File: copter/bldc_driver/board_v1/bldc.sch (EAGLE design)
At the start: 86 parts, among them IC1 LM339APWR, IC2 7411, IC3 7411, IC4 CD4051BPWR, IC5 FAN7388, Y1 16MHz

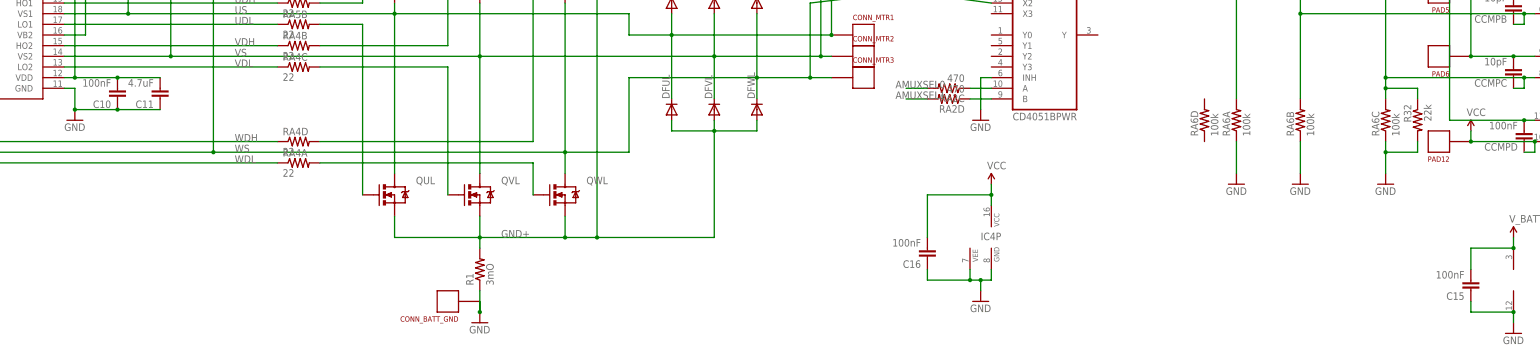
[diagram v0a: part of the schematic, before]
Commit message: simple arduino makefile
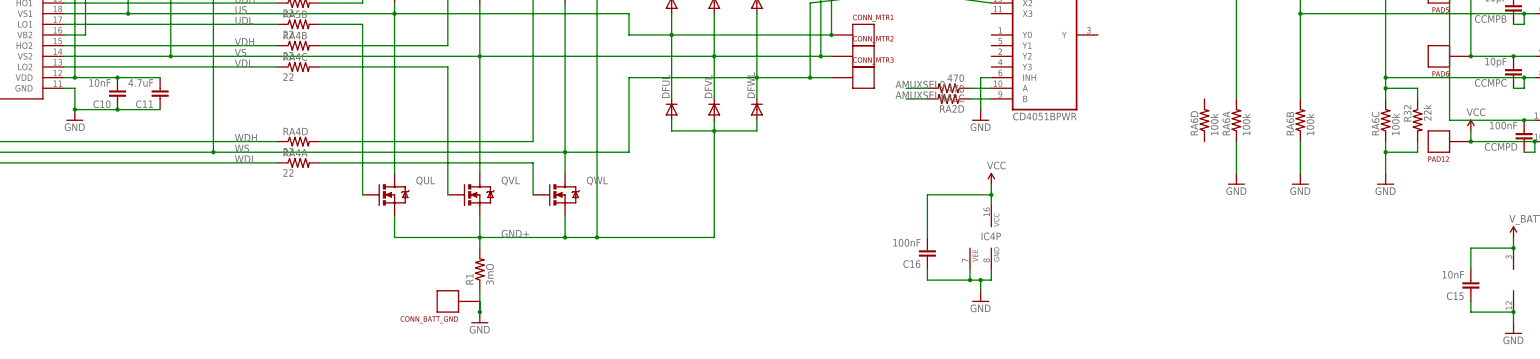
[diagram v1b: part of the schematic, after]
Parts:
- C10, C15: value 100nF -> 10nF
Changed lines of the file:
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@@
 <grid distance="0.1" unitdist="inch" unit="inch" style="lines" multiple="1" display="no" altdistance="0.01" altunitdist="inch" altunit="inch"/>
 <layers>
-<layer number="1" name="Top" color="4" fill="1" visible="yes" active="no"/>
-<layer number="16" name="Bottom" color="1" fill="1" visible="yes" active="no"/>
-<layer number="17" name="Pads" color="2" fill="1" visible="yes" active="no"/>
-<layer number="18" name="Vias" color="2" fill="1" visible="yes" active="no"/>
-<layer number="19" name="Unrouted" color="6" fill="1" visible="yes" active="no"/>
-<layer number="20" name="Dimension" color="15" fill="1" visible="yes" active="no"/>
-<layer number="21" name="tPlace" color="16" fill="1" visible="yes" active="no"/>
-<layer number="22" name="bPlace" color="14" fill="1" visible="yes" active="no"/>
-<layer number="23" name="tOrigins" color="15" fill="1" visible="yes" active="no"/>
-<layer number="24" name="bOrigins" color="15" fill="1" visible="yes" active="no"/>
-<layer number="25" name="tNames" color="7" fill="1" visible="yes" active="no"/>
-<layer number="26" name="bNames" color="7" fill="1" visible="yes" active="no"/>
-<layer number="27" name="tValues" color="7" fill="1" visible="yes" active="no"/>
-<layer number="28" name="bValues" color="7" fill="1" visible="yes" active="no"/>
+<layer number="1" name="Top" color="4" fill="1" visible="no" active="no"/>
+<layer number="16" name="Bottom" color="1" fill="1" visible="no" active="no"/>
+<layer number="17" name="Pads" color="2" fill="1" visible="no" active="no"/>
+<layer number="18" name="Vias" color="2" fill="1" visible="no" active="no"/>
+<layer number="19" name="Unrouted" color="6" fill="1" visible="no" active="no"/>
+<layer number="20" name="Dimension" color="15" fill="1" visible="no" active="no"/>
+<layer number="21" name="tPlace" color="16" fill="1" visible="no" active="no"/>
+<layer number="22" name="bPlace" color="14" fill="1" visible="no" active="no"/>
+<layer number="23" name="tOrigins" color="15" fill="1" visible="no" active="no"/>
+<layer number="24" name="bOrigins" color="15" fill="1" visible="no" active="no"/>
+<layer number="25" name="tNames" color="7" fill="1" visible="no" active="no"/>
+<layer number="26" name="bNames" color="7" fill="1" visible="no" active="no"/>
+<layer number="27" name="tValues" color="7" fill="1" visible="no" active="no"/>
+<layer number="28" name="bValues" color="7" fill="1" visible="no" active="no"/>
 <layer number="29" name="tStop" color="7" fill="3" visible="no" active="no"/>
 <layer number="30" name="bStop" color="7" fill="6" visible="no" active="no"/>
@@
 <layer number="35" name="tGlue" color="7" fill="4" visible="no" active="no"/>
 <layer number="36" name="bGlue" color="7" fill="5" visible="no" active="no"/>
-<layer number="37" name="tTest" color="7" fill="1" visible="yes" active="no"/>
-<layer number="38" name="bTest" color="7" fill="1" visible="yes" active="no"/>
+<layer number="37" name="tTest" color="7" fill="1" visible="no" active="no"/>
+<layer number="38" name="bTest" color="7" fill="1" visible="no" active="no"/>
 <layer number="39" name="tKeepout" color="4" fill="11" visible="no" active="no"/>
 <layer number="40" name="bKeepout" color="1" fill="11" visible="no" active="no"/>
@@
 <layer number="44" name="Drills" color="7" fill="1" visible="no" active="no"/>
 <layer number="45" name="Holes" color="7" fill="1" visible="no" active="no"/>
-<layer number="46" name="Milling" color="3" fill="1" visible="yes" active="no"/>
-<layer number="47" name="Measures" color="7" fill="1" visible="yes" active="no"/>
-<layer number="48" name="Document" color="7" fill="1" visible="yes" active="no"/>
-<layer number="49" name="Reference" color="7" fill="1" visible="yes" active="no"/>
-<layer number="50" name="dxf" color="7" fill="1" visible="yes" active="no"/>
-<layer number="51" name="tDocu" color="6" fill="1" visible="yes" active="no"/>
-<layer number="52" name="bDocu" color="7" fill="1" visible="yes" active="no"/>
-<layer number="53" name="tGND_GNDA" color="7" fill="9" visible="yes" active="no"/>
-<layer number="54" name="bGND_GNDA" color="1" fill="9" visible="yes" active="no"/>
-<layer number="56" name="wert" color="7" fill="1" visible="yes" active="no"/>
+<layer number="46" name="Milling" color="3" fill="1" visible="no" active="no"/>
+<layer number="47" name="Measures" color="7" fill="1" visible="no" active="no"/>
+<layer number="48" name="Document" color="7" fill="1" visible="no" active="no"/>
+<layer number="49" name="Reference" color="7" fill="1" visible="no" active="no"/>
+<layer number="50" name="dxf" color="7" fill="1" visible="no" active="no"/>
+<layer number="51" name="tDocu" color="6" fill="1" visible="no" active="no"/>
+<layer number="52" name="bDocu" color="7" fill="1" visible="no" active="no"/>
+<layer number="53" name="tGND_GNDA" color="7" fill="9" visible="no" active="no"/>
+<layer number="54" name="bGND_GNDA" color="1" fill="9" visible="no" active="no"/>
+<layer number="56" name="wert" color="7" fill="1" visible="no" active="no"/>
 <layer number="91" name="Nets" color="2" fill="1" visible="yes" active="yes"/>
 <layer number="92" name="Busses" color="1" fill="1" visible="yes" active="yes"/>
@@
 <part name="GND11" library="SparkFun-Aesthetics" deviceset="GND" device=""/>
 <part name="GND12" library="SparkFun-Aesthetics" deviceset="GND" device=""/>
-<part name="C10" library="SparkFun-Capacitors" deviceset="10NF-CER" device="" value="100nF"/>
+<part name="C10" library="SparkFun-Capacitors" deviceset="10NF-CER" device="" value="10nF"/>
 <part name="C11" library="SparkFun-Capacitors" deviceset="22UF-6.3V-20%(0805)" device="" value="4.7uF"/>
 <part name="C12" library="SparkFun-Capacitors" deviceset="22UF-6.3V-20%(0805)" device="" value="4.7uF">
@@
 <part name="GND21" library="SparkFun-Aesthetics" deviceset="GND" device=""/>
 <part name="SUPPLY12" library="SparkFun-Aesthetics" deviceset="V_BATT" device=""/>
-<part name="C15" library="SparkFun-Capacitors" deviceset="10NF-CER" device="" value="100nF"/>
+<part name="C15" library="SparkFun-Capacitors" deviceset="10NF-CER" device="" value="10nF"/>
 <part name="SUPPLY13" library="SparkFun-Aesthetics" deviceset="VCC" device=""/>
 <part name="R24" library="SparkFun-Resistors" deviceset="RESISTOR" device="0603-RES" value="10k"/>

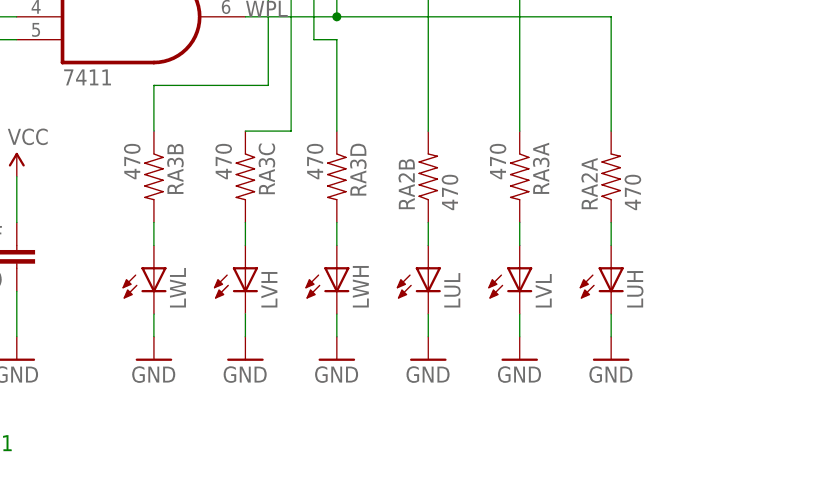
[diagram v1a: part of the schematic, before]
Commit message: fix some of the names in the bldc eagle files; update driver firmware to work with new board
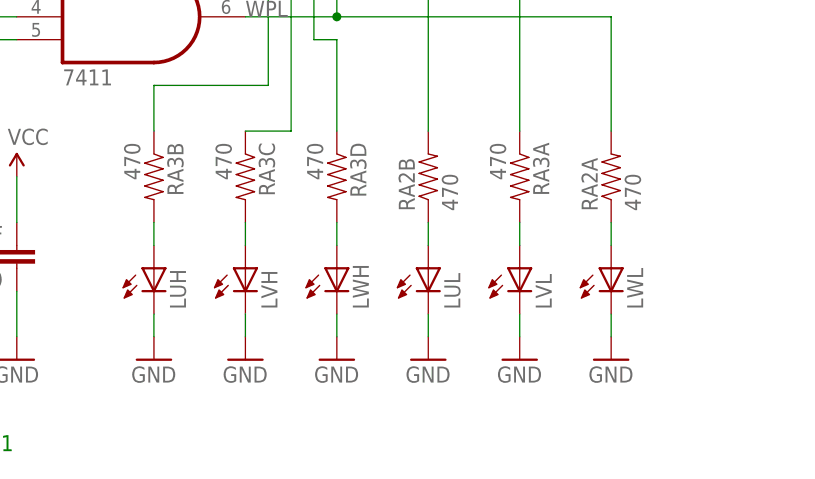
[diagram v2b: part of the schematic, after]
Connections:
- net N$8: now also LUH.A; no longer LWL.A
- net N$9: now also LWL.A; no longer LUH.A
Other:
- moved on the sheet: LUH, LWL
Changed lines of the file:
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@@
 <part name="SUPPLY10" library="SparkFun-Aesthetics" deviceset="V_BATT" device=""/>
 <part name="SUPPLY11" library="SparkFun-Aesthetics" deviceset="V_BATT" device=""/>
-<part name="LUH" library="kmod" deviceset="LED" device="0603" value=""/>
+<part name="LWL" library="kmod" deviceset="LED" device="0603" value=""/>
 <part name="GND15" library="SparkFun-Aesthetics" deviceset="GND" device=""/>
 <part name="LVH" library="kmod" deviceset="LED" device="0603" value=""/>
@@
 <part name="LVL" library="kmod" deviceset="LED" device="0603" value=""/>
 <part name="GND19" library="SparkFun-Aesthetics" deviceset="GND" device=""/>
-<part name="LWL" library="kmod" deviceset="LED" device="0603" value=""/>
+<part name="LUH" library="kmod" deviceset="LED" device="0603" value=""/>
 <part name="GND20" library="SparkFun-Aesthetics" deviceset="GND" device=""/>
 <part name="IC1" library="kmod" deviceset="LM339" device="" value="LM339APWR"/>
@@
 <instance part="SUPPLY10" gate="G$1" x="345.44" y="83.82"/>
 <instance part="SUPPLY11" gate="G$1" x="401.32" y="68.58"/>
-<instance part="LUH" gate="G$1" x="223.52" y="-17.78"/>
+<instance part="LWL" gate="G$1" x="223.52" y="-17.78"/>
 <instance part="GND15" gate="1" x="172.72" y="-27.94"/>
 <instance part="LVH" gate="G$1" x="182.88" y="-17.78"/>
@@
 <instance part="LVL" gate="G$1" x="213.36" y="-17.78"/>
 <instance part="GND19" gate="1" x="213.36" y="-27.94"/>
-<instance part="LWL" gate="G$1" x="172.72" y="-17.78"/>
+<instance part="LUH" gate="G$1" x="172.72" y="-17.78"/>
 <instance part="GND20" gate="1" x="223.52" y="-27.94"/>
 <instance part="IC1" gate="A" x="604.52" y="76.2"/>
@@
 </segment>
 <segment>
-<pinref part="LWL" gate="G$1" pin="C"/>
+<pinref part="LUH" gate="G$1" pin="C"/>
 <pinref part="GND15" gate="1" pin="GND"/>
 <wire x1="172.72" y1="-22.86" x2="172.72" y2="-25.4" width="0.1524" layer="91"/>
 </segment>
 <segment>
-<pinref part="LUH" gate="G$1" pin="C"/>
+<pinref part="LWL" gate="G$1" pin="C"/>
 <pinref part="GND20" gate="1" pin="GND"/>
 <wire x1="223.52" y1="-22.86" x2="223.52" y2="-25.4" width="0.1524" layer="91"/>
@@
 <net name="N$8" class="0">
 <segment>
-<pinref part="LWL" gate="G$1" pin="A"/>
+<pinref part="LUH" gate="G$1" pin="A"/>
 <pinref part="RA3" gate="B" pin="2"/>
 <wire x1="172.72" y1="-15.24" x2="172.72" y2="-12.7" width="0.1524" layer="91"/>
@@
 <net name="N$9" class="0">
 <segment>
-<pinref part="LUH" gate="G$1" pin="A"/>
+<pinref part="LWL" gate="G$1" pin="A"/>
 <pinref part="RA2" gate="A" pin="1"/>
 <wire x1="223.52" y1="-15.24" x2="223.52" y2="-12.7" width="0.1524" layer="91"/>

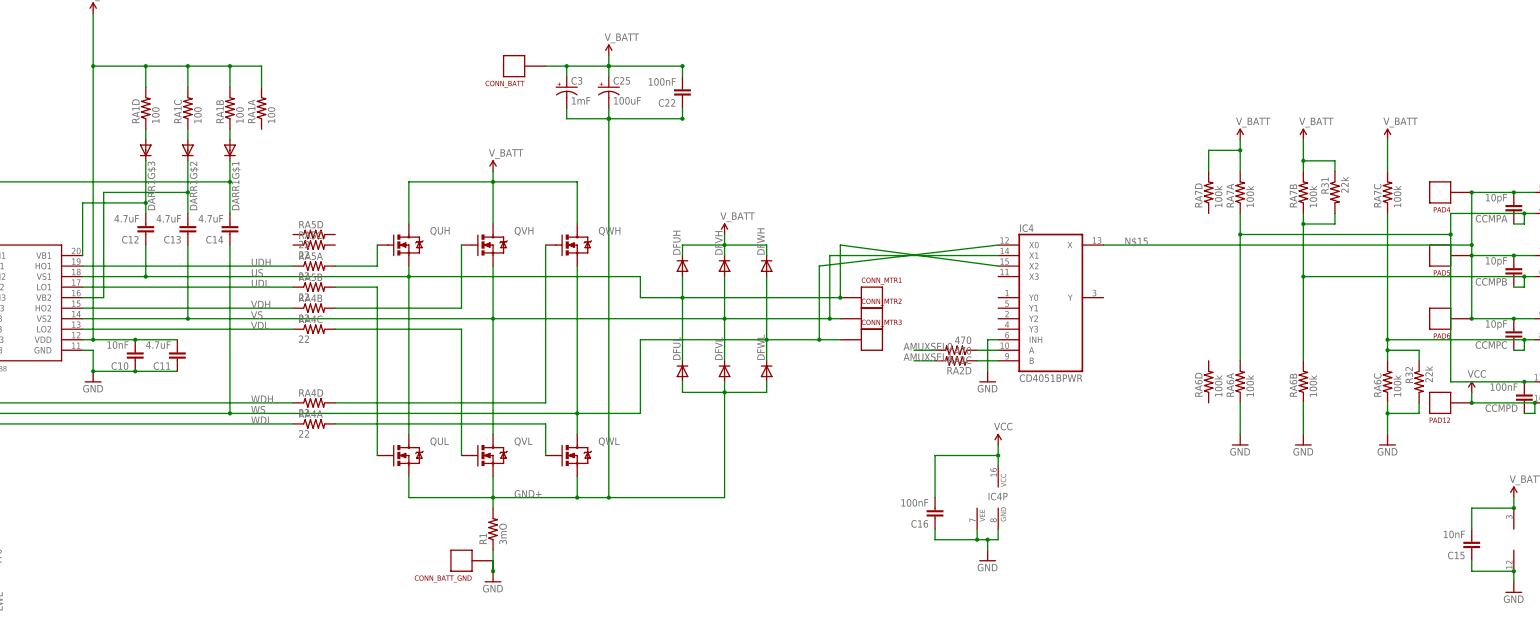
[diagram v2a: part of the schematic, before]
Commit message: changed some of the bldc board values
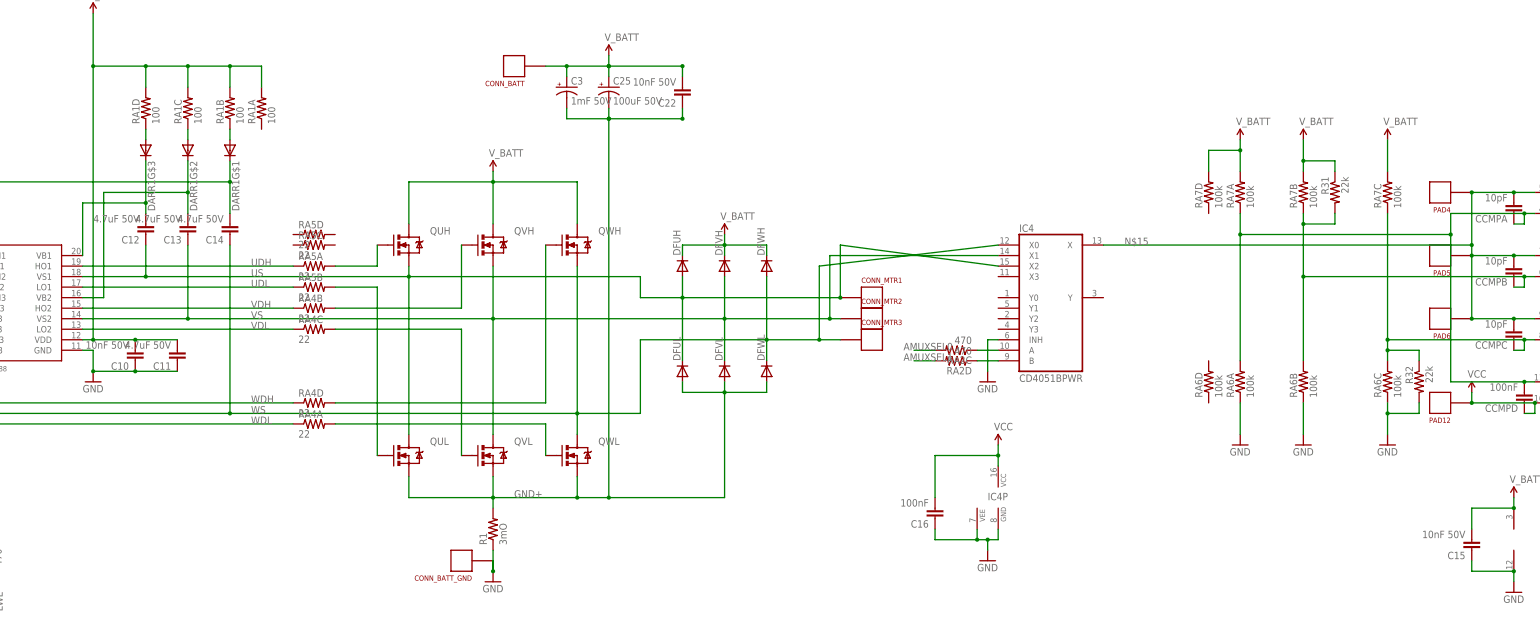
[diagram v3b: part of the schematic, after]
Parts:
- C10, C15: value 10nF -> 10nF 50V
- C11, C12, C13, C14: value 4.7uF -> 4.7uF 50V
- C22: value 100nF -> 10nF 50V
- C25: value 100uF -> 100uF 50V
- C3: value 1mF -> 1mF 50V
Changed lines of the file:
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@@
 <part name="GND11" library="SparkFun-Aesthetics" deviceset="GND" device=""/>
 <part name="GND12" library="SparkFun-Aesthetics" deviceset="GND" device=""/>
-<part name="C10" library="SparkFun-Capacitors" deviceset="10NF-CER" device="" value="10nF"/>
-<part name="C11" library="SparkFun-Capacitors" deviceset="22UF-6.3V-20%(0805)" device="" value="4.7uF"/>
-<part name="C12" library="SparkFun-Capacitors" deviceset="22UF-6.3V-20%(0805)" device="" value="4.7uF">
+<part name="C10" library="SparkFun-Capacitors" deviceset="10NF-CER" device="" value="10nF 50V"/>
+<part name="C11" library="SparkFun-Capacitors" deviceset="22UF-6.3V-20%(0805)" device="" value="4.7uF 50V"/>
+<part name="C12" library="SparkFun-Capacitors" deviceset="22UF-6.3V-20%(0805)" device="" value="4.7uF 50V">
 <attribute name="VOLTAGE" value="40"/>
 </part>
-<part name="C13" library="SparkFun-Capacitors" deviceset="22UF-6.3V-20%(0805)" device="" value="4.7uF">
+<part name="C13" library="SparkFun-Capacitors" deviceset="22UF-6.3V-20%(0805)" device="" value="4.7uF 50V">
 <attribute name="VOLTAGE" value="40"/>
 </part>
-<part name="C14" library="SparkFun-Capacitors" deviceset="22UF-6.3V-20%(0805)" device="" value="4.7uF">
+<part name="C14" library="SparkFun-Capacitors" deviceset="22UF-6.3V-20%(0805)" device="" value="4.7uF 50V">
 <attribute name="VOLTAGE" value="40"/>
 </part>
@@
 <part name="GND21" library="SparkFun-Aesthetics" deviceset="GND" device=""/>
 <part name="SUPPLY12" library="SparkFun-Aesthetics" deviceset="V_BATT" device=""/>
-<part name="C15" library="SparkFun-Capacitors" deviceset="10NF-CER" device="" value="10nF"/>
+<part name="C15" library="SparkFun-Capacitors" deviceset="10NF-CER" device="" value="10nF 50V"/>
 <part name="SUPPLY13" library="SparkFun-Aesthetics" deviceset="VCC" device=""/>
 <part name="R24" library="SparkFun-Resistors" deviceset="RESISTOR" device="0603-RES" value="10k"/>
@@
 <part name="CCMPC" library="SparkFun-Capacitors" deviceset="10NF-CER" device="" value="10pF"/>
 <part name="SUPPLY19" library="SparkFun-Aesthetics" deviceset="V_BATT" device=""/>
-<part name="C22" library="SparkFun-Capacitors" deviceset="10NF-CER" device="" value="100nF"/>
+<part name="C22" library="SparkFun-Capacitors" deviceset="10NF-CER" device="" value="10nF 50V"/>
 <part name="PAD4" library="kmod" deviceset="CONNECTOR" device="" value="CMPA"/>
 <part name="PAD5" library="kmod" deviceset="CONNECTOR" device="" value="CMPB"/>
@@
 <part name="QWH" library="kmod" deviceset="NXP_LFPAK_NFET" device=""/>
 <part name="DARR1" library="kmod" deviceset="SD103ATW-7-F" device=""/>
-<part name="C3" library="kmod" deviceset="CAP_POL" device="PTH5" value="1mF"/>
-<part name="C25" library="kmod" deviceset="CAP_POL" device="PTH1" value="100uF"/>
+<part name="C3" library="kmod" deviceset="CAP_POL" device="PTH5" value="1mF 50V"/>
+<part name="C25" library="kmod" deviceset="CAP_POL" device="PTH1" value="100uF 50V"/>
 <part name="CONN_BATT" library="kmod" deviceset="CONNECTOR" device="18AWG"/>
 <part name="CONN_BATT_GND" library="kmod" deviceset="CONNECTOR" device="18AWG"/>

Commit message: update values based on board #1
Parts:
- LD1: value LED0603 -> WHT
- LD13: value LED0603 -> BLUE
- LP5V: value LED0603 -> YELLOW
- LPBAT: value LED0603 -> GRN
- R6: value 470 -> 1k
- RA9: value 1k -> 2.2k
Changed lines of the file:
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@@
 <part name="S1" library="SparkFun-Electromechanical" deviceset="TAC_SWITCH" device="PTH"/>
 <part name="GND6" library="SparkFun-Aesthetics" deviceset="GND" device=""/>
-<part name="R6" library="SparkFun-Resistors" deviceset="RESISTOR" device="0603-RES" value="470"/>
-<part name="LD13" library="kmod" deviceset="LED" device="0603" value=""/>
+<part name="R6" library="SparkFun-Resistors" deviceset="RESISTOR" device="0603-RES" value="1k"/>
+<part name="LD13" library="kmod" deviceset="LED" device="0603" value="BLUE"/>
 <part name="GND7" library="SparkFun-Aesthetics" deviceset="GND" device=""/>
 <part name="R7" library="SparkFun-Resistors" deviceset="RESISTOR" device="0603-RES" value="470"/>
-<part name="LP5V" library="kmod" deviceset="LED" device="0603" value=""/>
+<part name="LP5V" library="kmod" deviceset="LED" device="0603" value="YELLOW"/>
 <part name="GND8" library="SparkFun-Aesthetics" deviceset="GND" device=""/>
-<part name="LPBAT" library="kmod" deviceset="LED" device="0603" value=""/>
+<part name="LPBAT" library="kmod" deviceset="LED" device="0603" value="GRN"/>
 <part name="GND9" library="SparkFun-Aesthetics" deviceset="GND" device=""/>
 <part name="SUPPLY6" library="SparkFun-Aesthetics" deviceset="VCC" device=""/>
@@
 <part name="PAD11" library="kmod" deviceset="CONNECTOR" device="" value="PD1"/>
 <part name="PAD12" library="kmod" deviceset="CONNECTOR" device="" value="VREF"/>
-<part name="LD1" library="kmod" deviceset="LED" device="0603" value=""/>
+<part name="LD1" library="kmod" deviceset="LED" device="0603" value="WHT"/>
 <part name="GND13" library="SparkFun-Aesthetics" deviceset="GND" device=""/>
-<part name="RA9" library="kmod" deviceset="RESISTOR_ARRAY" device="0603_X4" value="1k"/>
+<part name="RA9" library="kmod" deviceset="RESISTOR_ARRAY" device="0603_X4" value="2.2k"/>
 <part name="SUPPLY4" library="SparkFun-Aesthetics" deviceset="V_BATT" device=""/>
 </parts>
